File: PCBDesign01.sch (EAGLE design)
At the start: 14 parts, among them IC1 TESEO-LIV3R, U2 VX7805-500

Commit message: more stuff
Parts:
- removed D1: WL-SMCW-150060GS75000-G, WL-SMCW:WL-SMCW-150060GS75000-G
- removed LS1: PS1240P02BT, PS1240P02BT:PS1240P02BT
- added BUZZER: PS1240P02BT, PS1240P02BT:PS1240P02BT
- added C4, C5: (no value), Capacitor:C_CHIP-0805(2012-METRIC)
- added D2: CLX6F-FKC-CKNNQDGBB7A363, CLX6F-FKC-CKNNQDGBB7A363:CLX6F-FKC-CKNNQDGBB7A363
- added IND, LEDB, LEDG, LEDR, R2: (no value), Resistor:R-US_CHIP-0805(2012-METRIC)
- added J1: 5051102491, 5051102491:5051102491
- added PWR-INDICATOR: WL-SMCW-150060GS75000-G, WL-SMCW:WL-SMCW-150060GS75000-G
- C1, C2, C3: value C_CHIP-0805(2012-METRIC) -> (none)
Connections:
- new net N$1: D2.3, LEDR.1
- new net N$2: D2.2, LEDG.1
- new net N$4: D2.1, LEDB.1
- new net N$6: IND.1, PWR-INDICATOR.-
- new net N$7: J1.17, R2.1
- new net N$8: C5.1, J1.14
- new net N$9: C4.1, J1.8
- net GND: now also BUZZER.2, C4.2, C5.2, IND.2, J1.10, J1.23, J1.25, J1.26, LEDB.2, LEDG.2, LEDR.2, R2.2
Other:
- moved on the sheet: C1, C2, C3, IC1

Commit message: more stuff
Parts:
- removed IND: (no value), Resistor:R-US_CHIP-0805(2012-METRIC)
- added C10: 4.7uF, Capacitor:C_CHIP-0805(2012-METRIC)
- added C11: 0.1uF, Capacitor:C_CHIP-0805(2012-METRIC)
- added C6, C7, C8, C9: 1uF, Capacitor:C_CHIP-0805(2012-METRIC)
- added R10, R11, R12, R13, R8, R9: 0, Resistor:R-US_CHIP-0805(2012-METRIC)
- added R3: 87, Resistor:R-US_CHIP-0805(2012-METRIC)
- added R4, R6, R7: 10k, Resistor:R-US_CHIP-0805(2012-METRIC)
- added R5: 3.3K, Resistor:R-US_CHIP-0805(2012-METRIC)
- added U$5: 74LVC07APW, 74LVC07APW:74LVC07APW
- added U$6: ESP-PROG_JTAG_HEADER, ESP-PROG:ESP-PROG_JTAG_HEADER
- added U$7: ESP-PROG_PROGRAM_HEADER, ESP-PROG:ESP-PROG_PROGRAM_HEADER
- added U$8: (no value), Button:BUTTON
- added U1: TPS71913-28DRVR, TPS71913-28DRVR:TPS71913-28DRVR
- C1, C2, C5: value (none) -> 0.1uF
- C3: value (none) -> 10nF
- C4: value (none) -> 4.7uF
- LEDB: value (none) -> 200
- LEDG: value (none) -> 230
- LEDR: value (none) -> 193
- R1: value (none) -> 10k
- R2: value (none) -> 3.3K
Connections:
- net SCL renamed I2C_SCL
- net SDA renamed I2C_SDA
- net SIN renamed SIG
- net WP renamed N$15
- removed net AD0: U$1.AD0/SDO
- removed net CD: U$3.CD
- removed net DAT0: U$3.DAT0
- removed net DAT1: U$3.DAT1
- removed net DAT2: U$3.DAT2
- removed net DAT3: U$3.CD/DAT3
- removed net FSYNC: U$1.FSYNC
- removed net N$7: J1.17, R2.1
- removed net N$8: C5.1, J1.14
- removed net N$9: C4.1, J1.8
- removed net SCK: U$3.CLK
- new net 1.3V: C9.2, J1.10
- new net 2.8V: C7.1, J1.4, U1.OUT2
- new net 2.8V1: C10.1
- new net 3.3V2: C8.1, U1.OUT1
- new net BUZZER: U$5.4A
- new net BUZZER_OUT: BUZZER.1, U$5.4Y
- new net CAM_I2C_SCL: A1.IO23, J1.5, R2.2
- new net CAM_I2C_SDA: A1.IO18, J1.3, R5.2
- new net CAM_PWDN: A1.IO26, J1.8
- new net CAM_RESET: A1.IO19, J1.6
- new net CAM_RESET1: R4.1
- new net CAM_RESET2: R6.1
- new net DVP_HREF: A1.IO27, J1.9
- new net DVP_PCLK: A1.IO25, J1.17
- new net DVP_VSYNC: A1.IO5, J1.7
- new net DVP_Y2: A1.IO34, J1.19
- new net DVP_Y3: J1.21, R9.2
- new net DVP_Y4: J1.22, R8.2
- new net DVP_Y5: A1.IO35, J1.20
- new net DVP_Y6: A1.SENSOR_VN, J1.18
- new net DVP_Y7: J1.16, R10.2
- new net DVP_Y8: A1.IO2, J1.14
- new net DVP_Y9: A1.SENSOR_VP, J1.12
- new net JTAG_TCK: A1.IO13, R9.1, U$6.ESP_TCK
- new net JTAG_TDI: A1.IO12, R10.1, U$6.ESP_TDI
- new net JTAG_TDO: A1.IO15, R11.1, U$6.ESP_TDO
- new net JTAG_TMS: A1.IO14, R8.1, U$6.ESP_TMS
- new net LEDB_OUT: D2.6, U$5.3Y
- new net LEDG_OUT: D2.5, U$5.2Y
- new net LEDR_OUT: D2.4, U$5.1Y
- new net LED_B: R11.2, U$5.3A
- new net LED_G: R13.1, U$5.2A
- new net LED_R: R12.1, U$5.1A
- new net N$21: A1.EXP, A1.GND
- new net N$23: U$7.GND
- new net N$31: A1.IO32
- new net N$32: A1.IO33
- new net PROGRAM_EN: U$7.ESP_EN
- new net PROGRAM_EN1: A1.EN, C11.2, R7.1, U$8.B
- new net PROGRAM_IO0: A1.IO0, U$7.ESP_IO0
- new net PROGRAM_RX: A1.RXD0, R12.2, U$7.ESP_RXD
- new net PROGRAM_TX: A1.TXD0, R13.2, U$7.ESP_TXD
- new net SD_CMD: A1.SCS/CMD, U$3.CMD
- new net SD_DAT0: A1.SDO/SD0, U$3.DAT0
- new net SD_DAT1: A1.SDI/SD1, U$3.DAT1
- new net SD_DAT2: A1.SHD/SD2, U$3.DAT2
- new net SD_DAT3: A1.SWP/SD3, U$3.CD/DAT3
- new net SD_SCK: A1.SCK/CLK, U$3.CLK
- new net XMCLK: A1.IO4, J1.13
- net 3.3V: now also C4.1, C5.1, C6.1, IC1.VBATT, J1.11, PWR-INDICATOR.+, R2.1, R5.1, R6.2, R7.2, U$6.VDD, U$7.VDD, U1.EN1, U1.EN2, U1.IN
- net 5V: now also U$5.VCC
- net GND: now also C10.2, C11.1, C6.2, C7.2, C8.2, C9.1, J1.15, J1.2, R3.2, R4.2, U$1.AD0/SDO, U$1.FSYNC, U$5.GND, U$6.GND@1, U$6.GND@2, U$6.GND@3, U$6.GND@4, U$8.A, U1.EPAD, U1.GND; no longer A1.GND, IC1.GND_RF_1, IND.2, J1.10, J1.23, R2.2, U$4.GND@2
- net N$5: now also IC1.GND_RF_1, U$4.GND@2; no longer U$3.CMD
- net N$6: now also R3.1; no longer IND.1
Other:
- note added: "3.3V to 1.3V, 2.8V"
- note added: "9.8V to 12.3V"
- note added: "Antenna Connector"
- note added: "Current R: 15mA G: 10mA B: 10mA"
- note added: "Debug Indicators"
- note added: "Debug Piezo Buzzer"
- note added: "ESP-PROG INTERFACE"
- note added: "ESP32-WROVER-IB"
- note added: "Forward Voltage R: 2.1V G: 2.7V B: 3.0V"
- note added: "GPS"
- note added: "I2C Address: 1101000"
- note added: "MPU6500 IMU"
- note added: "OV2640 Camera"
- note added: "Power Indicator LED Vf = 2V I = 15mA"
- note added: "Power Supply"
- note added: "SD Card"
- note added: "VBat to 3.3V 1000mA max"
- note added: "VBat to 5V 500mA max"
- moved on the sheet: A1, C1, C2, C3, C4, C5, D2, IC1, J1, LEDB, LEDG, LEDR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

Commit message: moar
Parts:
- removed R1: 10k, Resistor:R-US_CHIP-0805(2012-METRIC)
- removed R12, R13: 0, Resistor:R-US_CHIP-0805(2012-METRIC)
- added BACK-LEFT, BACK-RIGHT, FRONT-LEFT, FRONT-RIGHT: ESC, ESC:ESC
- added R15: 10k, Resistor:R-US_CHIP-0805(2012-METRIC)
- added U$10, U$11, U$12, U$13, U$14, U$15, U$16, U$17, U$18, U$19, U$20, U$21, U$22, U$23, U$24, U$25, U$26, U$27, U$9: TESTPOINT, Test Point:TESTPOINT
- added U3: CD40109BPWR, CD40109BPWR:CD40109BPWR
- added U4: FXL6408UMX, FXL6408UMX:FXL6408UMX
- U$8: value (none) -> RESET
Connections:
- removed net 2.8V1: C10.1
- removed net 3.3V2: C8.1, U1.OUT1
- removed net CAM_RESET1: R4.1
- removed net CAM_RESET2: R6.1
- removed net N$15: R1.2, U$3.WP
- removed net N$31: A1.IO32
- removed net N$32: A1.IO33
- removed net PROGRAM_EN1: A1.EN, C11.2, R7.1, U$8.B
- new net ESCL_BL: U3.ENABLE_C
- new net ESC_BL_OUT: U$25.0, U3.G
- new net ESC_BR: U3.ENABLE_D
- new net ESC_BR_OUT: U$27.0, U3.H
- new net ESC_FL: U3.ENABLE_B
- new net ESC_FL_OUT: FRONT-LEFT.SIG, U$26.0, U3.F
- new net ESC_FR: U3.ENABLE_A
- new net ESC_FR_OUT: FRONT-RIGHT.SIG, U$24.0, U3.E
- new net GPS_RX: A1.IO32, IC1.RX, U$11.0
- new net GPS_TX: A1.IO33, IC1.TX, U$12.0
- new net N$18: R11.2
- new net N$27: U4.GPIO4
- new net SD_CD: U$3.CD, U4.GPIO6
- new net SD_WP: U$3.WP, U4.GPIO7
- net 1.3V: now also C8.1, U$17.0, U1.OUT1
- net 2.8V: now also C10.1, U$18.0
- net 3.3V: now also R15.2, U$15.0, U3.VCC, U4.VCC, U4.VDDIO
- net 5V: now also BACK-LEFT.5V, BACK-RIGHT.5V, FRONT-LEFT.5V, FRONT-RIGHT.5V, U$16.0, U3.A, U3.B, U3.C, U3.D, U3.VDD
- net BUZZER: now also U4.GPIO3
- net CAM_PWDN: now also R4.1
- net CAM_RESET: now also R6.1
- net GND: now also A1.EXP, A1.GND, BACK-LEFT.GND, BACK-RIGHT.GND, FRONT-LEFT.GND, FRONT-RIGHT.GND, U$14.0, U$19.0, U$20.0, U$21.0, U$22.0, U$7.GND, U3.VSS, U4.ADDR, U4.GND; no longer R1.1
- net I2C_SCL: now also U$10.0, U4.SCL; no longer IC1.SCL
- net I2C_SDA: now also U$9.0, U4.SDA; no longer IC1.SDA
- net LED_B: now also U4.GPIO2; no longer R11.2
- net LED_G: now also U4.GPIO1; no longer R13.1
- net LED_R: now also U4.GPIO0; no longer R12.1
- net N$21: now also U4.GPIO5; no longer A1.EXP, A1.GND
- net N$23: now also R15.1, U4.!RST; no longer U$7.GND
- net PROGRAM_EN: now also A1.EN, C11.2, R7.1, U$23.0, U$8.B
- net PROGRAM_RX: no longer R12.2
- net PROGRAM_TX: no longer R13.2
- net VBAT: now also U$13.0
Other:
- note added: "3.3V to 5V Logic Level Shifter"
- note added: "Connects to 3-pin housing of ESC signal connector"
- note added: "ESC"
- note added: "Expandable I2C GPIO"
- note added: "Interrupt output, open-drain, requires an external pull-up resistor to Vcc Do I actually need that resistor if I don't use it???"
- moved on the sheet: A1, C1, C10, C11, C2, C3, C4, C5, C6, C7, C8, C9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

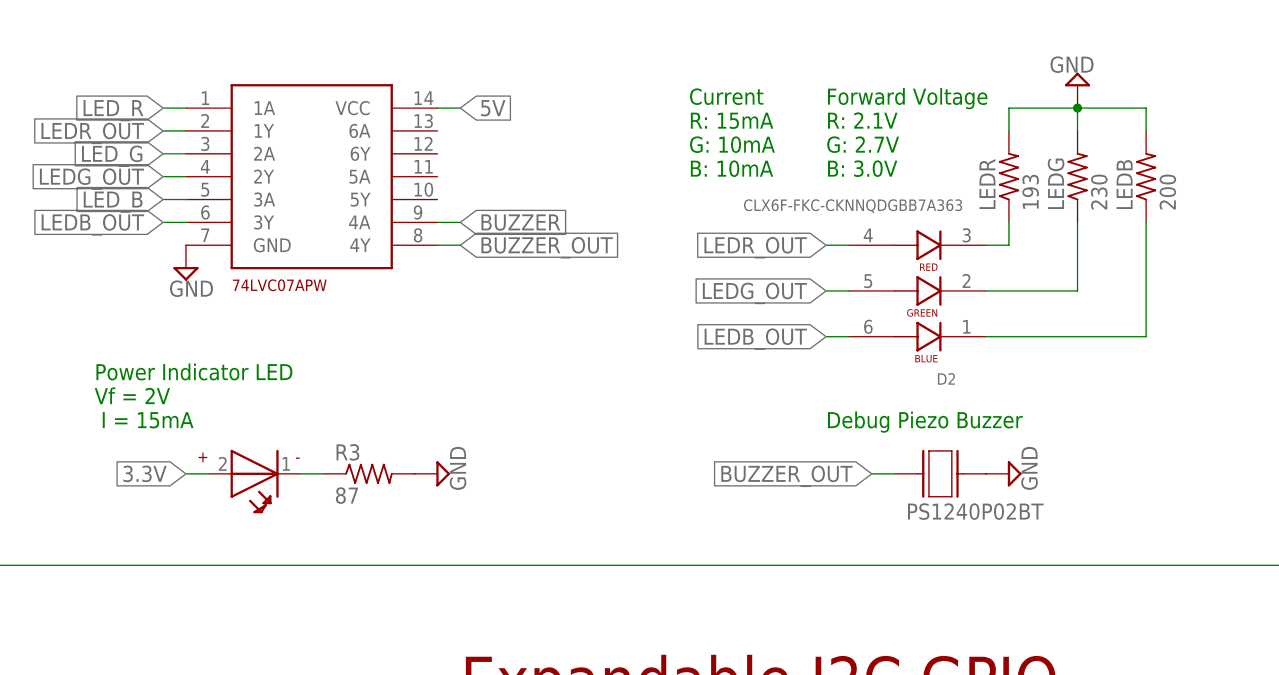
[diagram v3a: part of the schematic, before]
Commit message: minor resistor changes
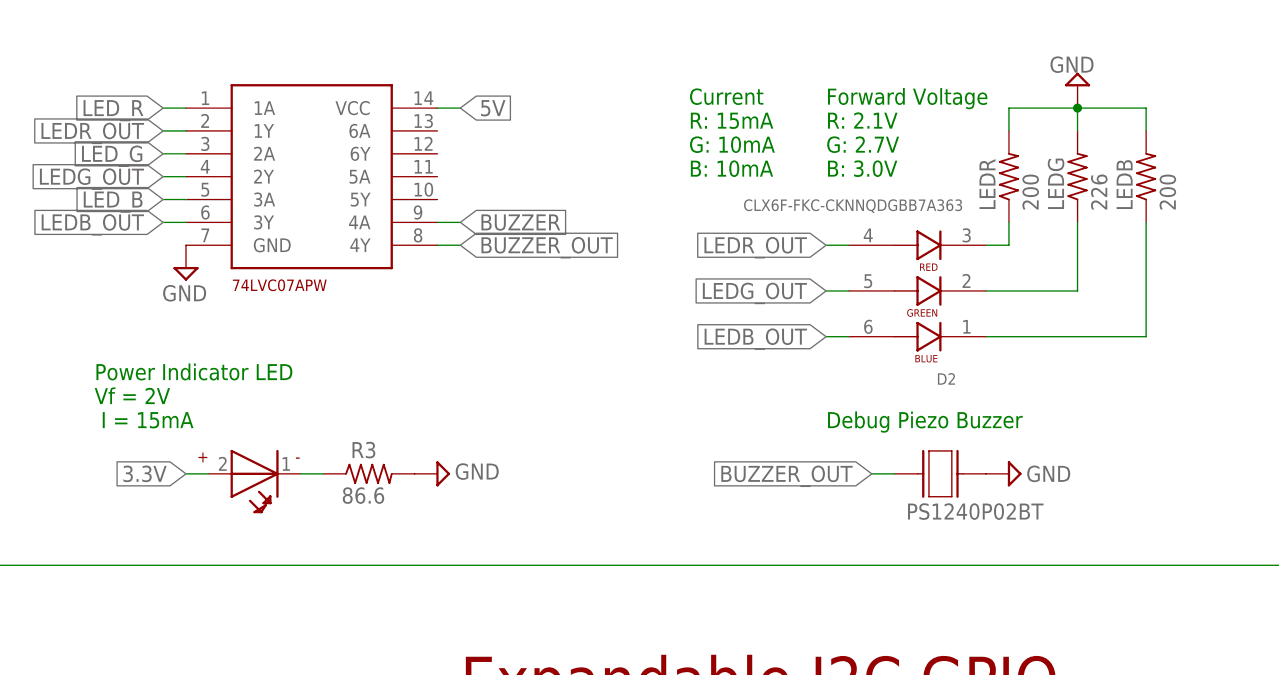
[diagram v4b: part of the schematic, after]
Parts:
- LEDG: value 230 -> 226
- LEDR: value 193 -> 200
- R3: value 87 -> 86.6
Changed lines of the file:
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@@
 <part name="D2" library="CLX6F-FKC-CKNNQDGBB7A363" deviceset="CLX6F-FKC-CKNNQDGBB7A363" device=""/>
 <part name="J1" library="5051102491" deviceset="5051102491" device=""/>
-<part name="LEDR" library="Resistor" library_urn="urn:adsk.eagle:library:16378527" deviceset="R-US" device="CHIP-0805(2012-METRIC)" package3d_urn="urn:adsk.eagle:package:16378559/2" technology="_" value="193"/>
-<part name="LEDG" library="Resistor" library_urn="urn:adsk.eagle:library:16378527" deviceset="R-US" device="CHIP-0805(2012-METRIC)" package3d_urn="urn:adsk.eagle:package:16378559/2" technology="_" value="230"/>
+<part name="LEDR" library="Resistor" library_urn="urn:adsk.eagle:library:16378527" deviceset="R-US" device="CHIP-0805(2012-METRIC)" package3d_urn="urn:adsk.eagle:package:16378559/2" technology="_" value="200"/>
+<part name="LEDG" library="Resistor" library_urn="urn:adsk.eagle:library:16378527" deviceset="R-US" device="CHIP-0805(2012-METRIC)" package3d_urn="urn:adsk.eagle:package:16378559/2" technology="_" value="226"/>
 <part name="LEDB" library="Resistor" library_urn="urn:adsk.eagle:library:16378527" deviceset="R-US" device="CHIP-0805(2012-METRIC)" package3d_urn="urn:adsk.eagle:package:16378559/2" technology="_" value="200"/>
-<part name="R3" library="Resistor" library_urn="urn:adsk.eagle:library:16378527" deviceset="R-US" device="CHIP-0805(2012-METRIC)" package3d_urn="urn:adsk.eagle:package:16378559/2" technology="_" value="87"/>
+<part name="R3" library="Resistor" library_urn="urn:adsk.eagle:library:16378527" deviceset="R-US" device="CHIP-0805(2012-METRIC)" package3d_urn="urn:adsk.eagle:package:16378559/2" technology="_" value="86.6"/>
 <part name="SUPPLY1" library="supply2" library_urn="urn:adsk.eagle:library:372" deviceset="GND" device=""/>
 <part name="SUPPLY6" library="supply2" library_urn="urn:adsk.eagle:library:372" deviceset="GND" device=""/>
@@
 </instance>
 <instance part="R3" gate="G$1" x="-200.66" y="-40.64" smashed="yes">
-<attribute name="NAME" x="-204.47" y="-39.1414" size="1.778" layer="95"/>
-<attribute name="VALUE" x="-204.47" y="-43.942" size="1.778" layer="96"/>
+<attribute name="NAME" x="-202.692" y="-38.8874" size="1.778" layer="95"/>
+<attribute name="VALUE" x="-203.708" y="-43.942" size="1.778" layer="96"/>
 </instance>
 <instance part="SUPPLY1" gate="GND" x="233.68" y="-25.4" smashed="yes">
@@
 </instance>
 <instance part="SUPPLY17" gate="GND" x="-193.04" y="-40.64" smashed="yes" rot="R90">
-<attribute name="VALUE" x="-189.865" y="-42.545" size="1.778" layer="96" rot="R90"/>
+<attribute name="VALUE" x="-191.135" y="-41.275" size="1.778" layer="96"/>
 </instance>
 <instance part="SUPPLY18" gate="GND" x="-129.54" y="-40.64" smashed="yes" rot="R90">
-<attribute name="VALUE" x="-126.365" y="-42.545" size="1.778" layer="96" rot="R90"/>
+<attribute name="VALUE" x="-127.635" y="-41.529" size="1.778" layer="96"/>
 </instance>
 <instance part="SUPPLY19" gate="GND" x="-121.92" y="2.54" smashed="yes" rot="R180">
@@
 <instance part="U$5" gate="G$1" x="-208.28" y="-10.16" smashed="yes"/>
 <instance part="SUPPLY21" gate="GND" x="-220.98" y="-17.78" smashed="yes">
-<attribute name="VALUE" x="-222.885" y="-20.955" size="1.778" layer="96"/>
+<attribute name="VALUE" x="-223.647" y="-21.463" size="1.778" layer="96"/>
 </instance>
 <instance part="SUPPLY22" gate="GND" x="76.2" y="-66.04" smashed="yes" rot="R90">

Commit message: pressure sensor
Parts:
- added C12, C13, C14, C15, C16: 10uF, Capacitor:C_CHIP-0805(2012-METRIC)
- added C17, C18, C19, C20, C21: 0.1uF, Capacitor:C_CHIP-0805(2012-METRIC)
- added R1: 1k, Resistor:R-US_CHIP-0805(2012-METRIC)
- added R12, R13, R18, R19, R20, R21: 10k, Resistor:R-US_CHIP-0805(2012-METRIC)
- added R14, R16, R17: 0, Resistor:R-US_CHIP-0805(2012-METRIC)
- C3: value 10nF -> 0.1uF
- U$5: value 74LVC07APW -> SPL06-007; device 74LVC07APW:74LVC07APW -> SPL06-007:SPL06-007
- U4: value FXL6408UMX -> MCP23017T-E/SO; device FXL6408UMX:FXL6408UMX -> MCP23017T-E_SO:MCP23017T-E/SO
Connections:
- removed net BUZZER_OUT: BUZZER.1, U$5.4Y
- removed net ESCL_BL: U3.ENABLE_C
- removed net LEDB_OUT: D2.6, U$5.3Y
- removed net LEDG_OUT: D2.5, U$5.2Y
- removed net LEDR_OUT: D2.4, U$5.1Y
- removed net N$21: U4.GPIO5
- removed net N$27: U4.GPIO4
- removed net SD_SCK: A1.SCK/CLK, U$3.CLK
- new net ESC_BL: U3.ENABLE_C, U4.GPB2
- new net N$19: R20.1, U4.A1
- new net N$20: R19.1, U4.A0
- new net SD_CLK: R8.2, U$3.CLK
- net 3.3V: now also C15.2, C16.2, C17.2, C19.2, C20.2, C21.2, R12.1, R13.1, R18.1, U$5.VDD, U$5.VDDIO, U4.VDD; no longer U4.VCC, U4.VDDIO
- net 5V: now also C14.2, C18.2; no longer U$5.VCC
- net BUZZER: now also BUZZER.1, R1.1, U4.GPA3; no longer U$5.4A, U4.GPIO3
- net CAM_PWDN: now also U4.GPB5; no longer A1.IO26
- net CAM_RESET: now also U4.GPB4; no longer A1.IO19
- net DVP_Y3: now also R14.2; no longer R9.2
- net DVP_Y4: now also R17.1; no longer R8.2
- net DVP_Y7: now also R16.1; no longer R10.2
- net DVP_Y8: now also A1.IO19; no longer A1.IO2
- net ESC_BR: now also U4.GPB3
- net ESC_FL: now also U4.GPB1
- net ESC_FR: now also U4.GPB0
- net GND: now also C12.1, C13.1, C14.1, C15.1, C16.1, C17.1, C18.1, C19.1, C20.1, C21.1, R1.2, R19.2, R20.2, R21.2, U$5.GND@1, U$5.GND@2, U4.VSS; no longer U$5.GND, U4.ADDR, U4.GND
- net I2C_SCL: now also U$5.SCK, U4.SCK; no longer U4.SCL
- net I2C_SDA: now also R18.2, U$5.SDA
- net LED_B: now also D2.6, U4.GPA2; no longer U$5.3A, U4.GPIO2
- net LED_G: now also D2.5, U4.GPA1; no longer U$5.2A, U4.GPIO1
- net LED_R: now also D2.4, U4.GPA0; no longer U$5.1A, U4.GPIO0
- net N$18: now also R21.1, U4.A2; no longer R11.2
- net N$23: now also U4.!RESET; no longer U4.!RST
- net PROGRAM_IO0: now also R14.1
- net PROGRAM_RX: now also R17.2
- net PROGRAM_TX: now also R16.2
- net SD_CD: now also U4.GPA5; no longer U4.GPIO6
- net SD_CMD: now also R11.2, R12.2; no longer A1.SCS/CMD
- net SD_DAT0: now also A1.IO2, R13.2; no longer A1.SDO/SD0
- net SD_DAT1: now also A1.IO4; no longer A1.SDI/SD1
- net SD_DAT2: now also R10.2; no longer A1.SHD/SD2
- net SD_DAT3: now also R9.2; no longer A1.SWP/SD3
- net SD_WP: now also U4.GPA4; no longer U4.GPIO7
- net VBAT: now also C12.2, C13.2
- net XMCLK: now also A1.IO26; no longer A1.IO4
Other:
- note added: "I2C Address: 0100000"
- note added: "I2C Address: 1110111"
- note added: "Pressure Sensor"
- note removed: "Interrupt output, open-drain, requires an external pull-up resistor to Vcc Do I actually need that resistor if I don't use it???"
- moved on the sheet: BACK-LEFT, BACK-RIGHT, C11, C6, C7, C8, D2, FRONT-LEFT, FRONT-RIGHT, LEDB, LEDG, LEDR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

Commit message: doing pcb layout
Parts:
- removed R19, R20, R21: 10k, Resistor:R-US_CHIP-0805(2012-METRIC)
- removed U$2: LARGE_BATTERY, CustomBattery:LARGE_BATTERY
- removed U2: VX7805-500, VX7805-500:VX7805-500
- added C22: 47pF, C0402C470K5GACTU:C0402C470K5GACTU
- added C23: 0.1uF, Capacitor:C_CHIP-0805(2012-METRIC)
- added L1: 39nH, 0402 Inductor:HK100539NJ-TIND0402_22N_TAI_TAY-M
- added U$28: AS78L05RTR-E1, AS78L05RTR-E1:AS78L05RTR-E1
- added U$29: LARGE_BATTERY, CustomBattery:LARGE_BATTERY
- LEDB: value 200 -> 30
- LEDG: value 226 -> 60
- LEDR: value 200 -> 80
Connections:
- removed net N$18: R21.1, U4.A2
- removed net N$19: R20.1, U4.A1
- removed net N$20: R19.1, U4.A0
- removed net N$5: IC1.GND_RF_1, U$4.GND@2
- removed net SIG: IC1.RF_IN, U$4.SIN
- new net ANT: C22.2, L1.2, U$4.SIN
- new net N$21: C22.1, IC1.RF_IN
- new net VCC_RF: C23.2, IC1.VCC_RF, L1.1
- net 3.3V: now also U3.ENABLE_A, U3.ENABLE_B, U3.ENABLE_C, U3.ENABLE_D
- net 5V: now also U$28.5V_OUT; no longer U2.+VOUT/GND, U3.A, U3.B, U3.C, U3.D
- net ESC_BL: now also U3.C; no longer U3.ENABLE_C
- net ESC_BL_OUT: now also BACK-LEFT.SIG
- net ESC_BR: now also U3.D; no longer U3.ENABLE_D
- net ESC_BR_OUT: now also BACK-RIGHT.SIG
- net ESC_FL: now also U3.B; no longer U3.ENABLE_B
- net ESC_FR: now also U3.A; no longer U3.ENABLE_A
- net GND: now also C23.1, IC1.GND_RF_1, U$28.GND, U$29.GND, U$4.GND@2, U4.A0, U4.A1, U4.A2; no longer R19.2, R20.2, R21.2, U$2.GND, U2.GND/-VOUT
- net VBAT: now also U$28.INPUT, U$29.V_BAT; no longer U$2.V_BAT, U2.+VIN
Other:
- note added: "VBat to 5V 100mA max"
- note removed: "VBat to 5V 500mA max"
- moved on the sheet: C13, C14, C15, PS1
